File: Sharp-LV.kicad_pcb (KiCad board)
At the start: 4 copper layers, 69.7 x 44.7 mm, 52 parts, among them J1 USB_C_Receptacle_USB2.0, J2 Conn_01x05_PROG, J3 5024260810, J4 FH52-10S-0.5SH_99, J5 SM04B-SRSS-TB_LF__SN_, J6 Conn_2Rows-13Pins, J7 S2B-PH-SM4-TB_LF__SN_, U1 NRF52840-QIAA-R, U2 USBLC6-2P6, U3 MCP1700-3302E_SOT23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

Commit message: Add GND pane
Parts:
- added R8: 5.1k, Resistor_SMD:R_0603_1608Metric, F.Cu at (114.8, 78.4)
- moved C20 0.31 mm to (112.4, 76.5)
- moved U2 0.10 mm to (115.5, 80.3)
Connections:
- J1 pad A5: unconnected-(J1-CC1-PadA5) -> Net-(J1-CC1)
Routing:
- net Net-(J1-CC1): track 0.00 -> 6.64 mm
- net VBUS: track 64.1 -> 63.3 mm
- net GND: track 58.2 -> 59.0 mm, vias 45 -> 46

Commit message: Update S3 routing proposal
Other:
- board text added: "VDD2_EN"
- board text added: "nRF52840"
- board text removed: "VDD_ENABLE"
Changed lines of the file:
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@@
     (property "ki_keywords" "test point tp")
     (attr exclude_from_pos_files exclude_from_bom)
-    (fp_text reference "TP3" (at 0 -1.648) (layer "F.SilkS")
+    (fp_text reference "TP3" (at -2.11 -1.15) (layer "F.SilkS")
         (effects (font (size 0.8 0.8) (thickness 0.14) bold))
     )
@@
     (property "ki_keywords" "test point tp")
     (attr exclude_from_pos_files exclude_from_bom)
-    (fp_text reference "TP1" (at -0.15 -1.59) (layer "F.SilkS")
+    (fp_text reference "TP1" (at -2.19 -0.02) (layer "F.SilkS")
         (effects (font (size 0.8 0.8) (thickness 0.15) bold))
     )
@@
     (zone_connect 2)
     (attr smd)
-    (fp_text reference "U1" (at -0.01 4.79 unlocked) (layer "F.SilkS")
+    (fp_text reference "U1" (at 5.23 3.23 unlocked) (layer "F.SilkS")
         (effects (font (size 1 1) (thickness 0.15)))
     )
@@
     (effects (font (size 1 1) (thickness 0.1)) (justify left bottom))
   )
+  (gr_text "nRF52840" (at 130.41 60.12) (layer "F.SilkS")
+    (effects (font (size 1.4 1.4) (thickness 0.2) bold) (justify left bottom))
+  )
   (gr_text "Enabled w/P1.07 HIGH" (at 148.62 86.9) (layer "F.SilkS")
     (effects (font (size 1 1) (thickness 0.1)) (justify left bottom))
@@
     (effects (font (size 1 1) (thickness 0.1)) (justify left bottom))
   )
-  (gr_text "VDD_ENABLE" (at 124.44 65.58) (layer "F.SilkS")
+  (gr_text "VDD2_EN" (at 128.75 64.3) (layer "F.SilkS")
     (effects (font (size 1 1) (thickness 0.1)) (justify left bottom))
   )

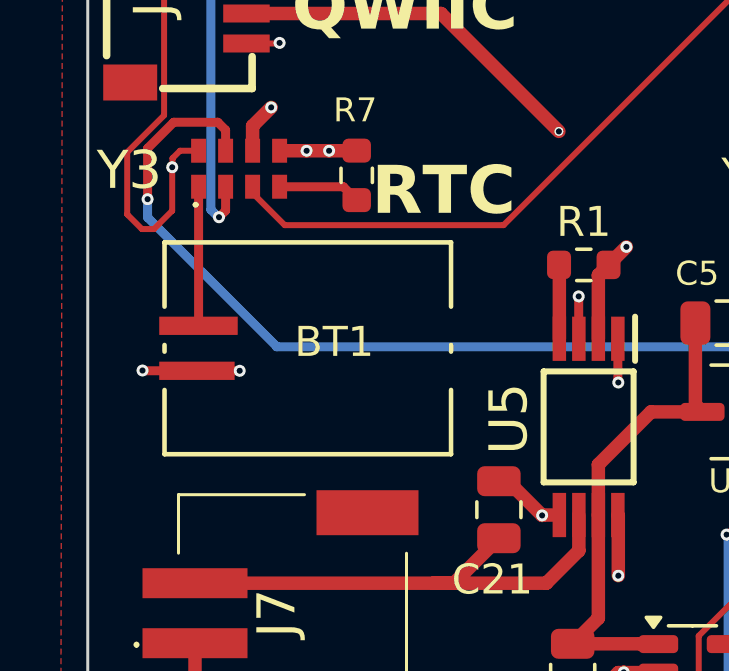
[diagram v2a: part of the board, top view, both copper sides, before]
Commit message: Update BT1 routing because bad polarity
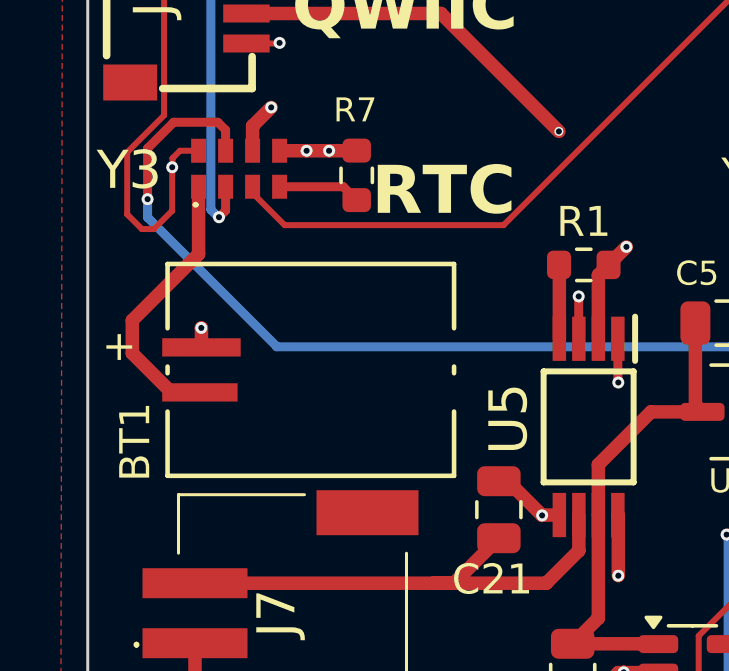
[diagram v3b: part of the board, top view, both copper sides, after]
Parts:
- moved BT1 0.73 mm to (106.7, 60.6)
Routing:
- net VDD_RTC: track 4.64 -> 9.26 mm
- net GND: track 59.0 -> 56.4 mm, vias 46 -> 45

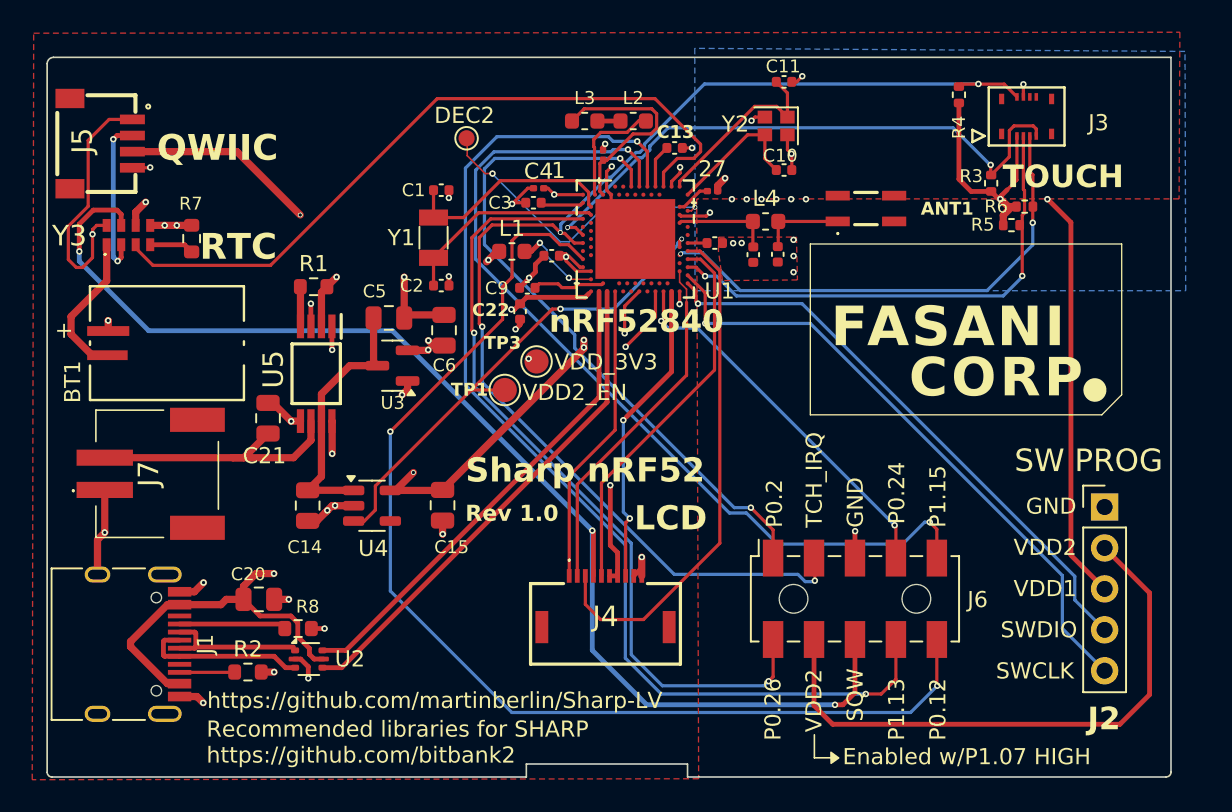
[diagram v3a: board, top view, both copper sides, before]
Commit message: Update TOUCH pinout in PCBs
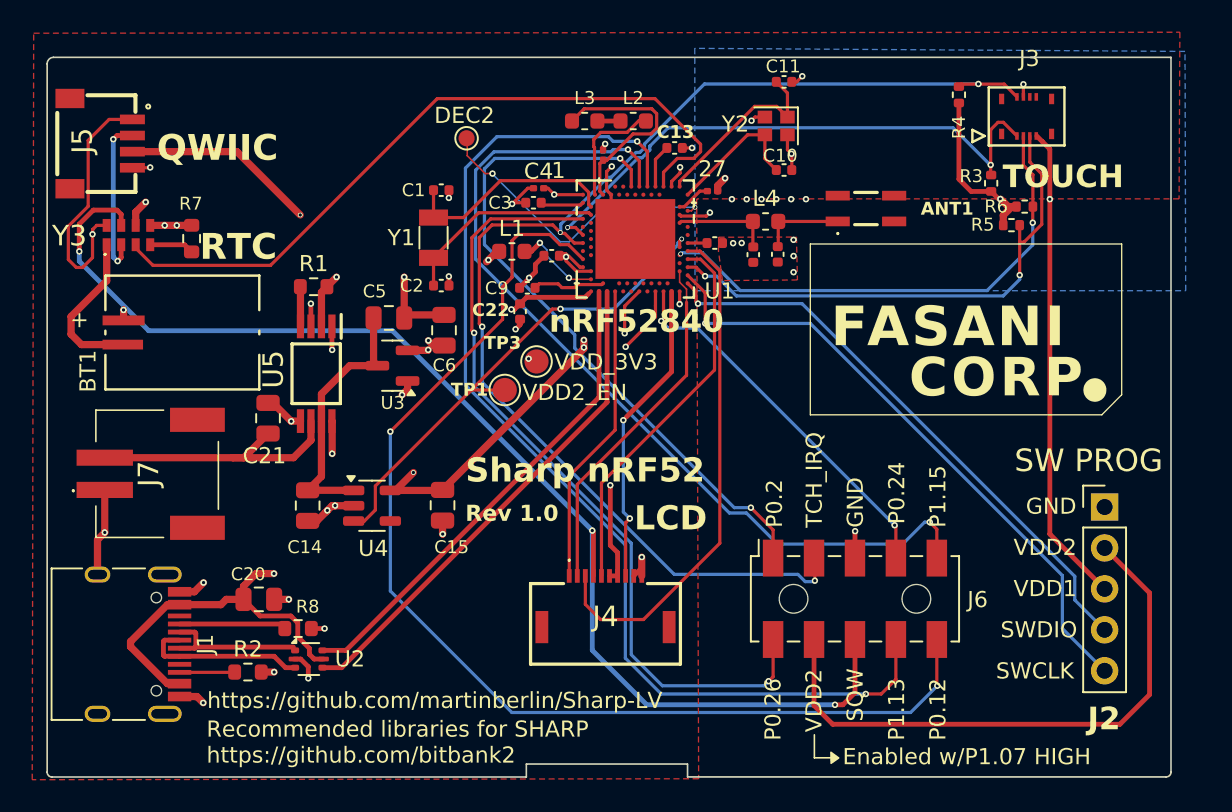
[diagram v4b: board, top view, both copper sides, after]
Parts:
- moved BT1 1.16 mm to (107.7, 60.0)
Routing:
- net /SDA: track 78.6 -> 80.5 mm
- net /TOUCH_REST: track 37.3 -> 36.1 mm
- net VDD_RTC: track 9.26 -> 9.94 mm
